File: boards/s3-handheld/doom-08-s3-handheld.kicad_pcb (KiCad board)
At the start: 4 copper layers, 156 x 66 mm, 62 parts, among them J2 S2B-PH-K-S(LF)(SN), J4 DM3AT-SF-PEJM5, J5 S2B-PH-K-S(LF)(SN), SW12 JS102011SAQN, U1 ESP32-S3-WROOM-1-N16R8, U2 ESD 2-line, U4 TLV75533PDBVR, U5 MAX98357AETE+T, U6 BQ24074RGTR, U7 MAX17048G+T10

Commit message: PCBKit's mark and pcbkit.io on every board; the RP2350 handheld ready to order
The handheld runs from two 18650 cells in parallel behind a DW01A protector and a reverse-cell
P-MOSFET, charged at up to 500 mA from the Pico's USB-C by a BQ24075 (power path into VSYS, timers
off for 6 Ah), with an on/off switch on 3V3_EN, M3 holes, ground pours and the console on pads.
Every assembled part has a JLCPCB code in stock (Basic where there is one); the module sockets are
in the BOM, the modules listed in the order's README. Check complete, the ready review clean.
Every board: routed and checked complete with the new mark.
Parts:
- added logo: , Logo_PCBKit_pcbkit.io, F.Cu at (209.5, 195.2)
- SW1, SW10, SW11, SW2, SW3, SW4, SW5, SW6, SW7, SW8, SW9: value (none) -> PTS645SM43SMTR92 LFS

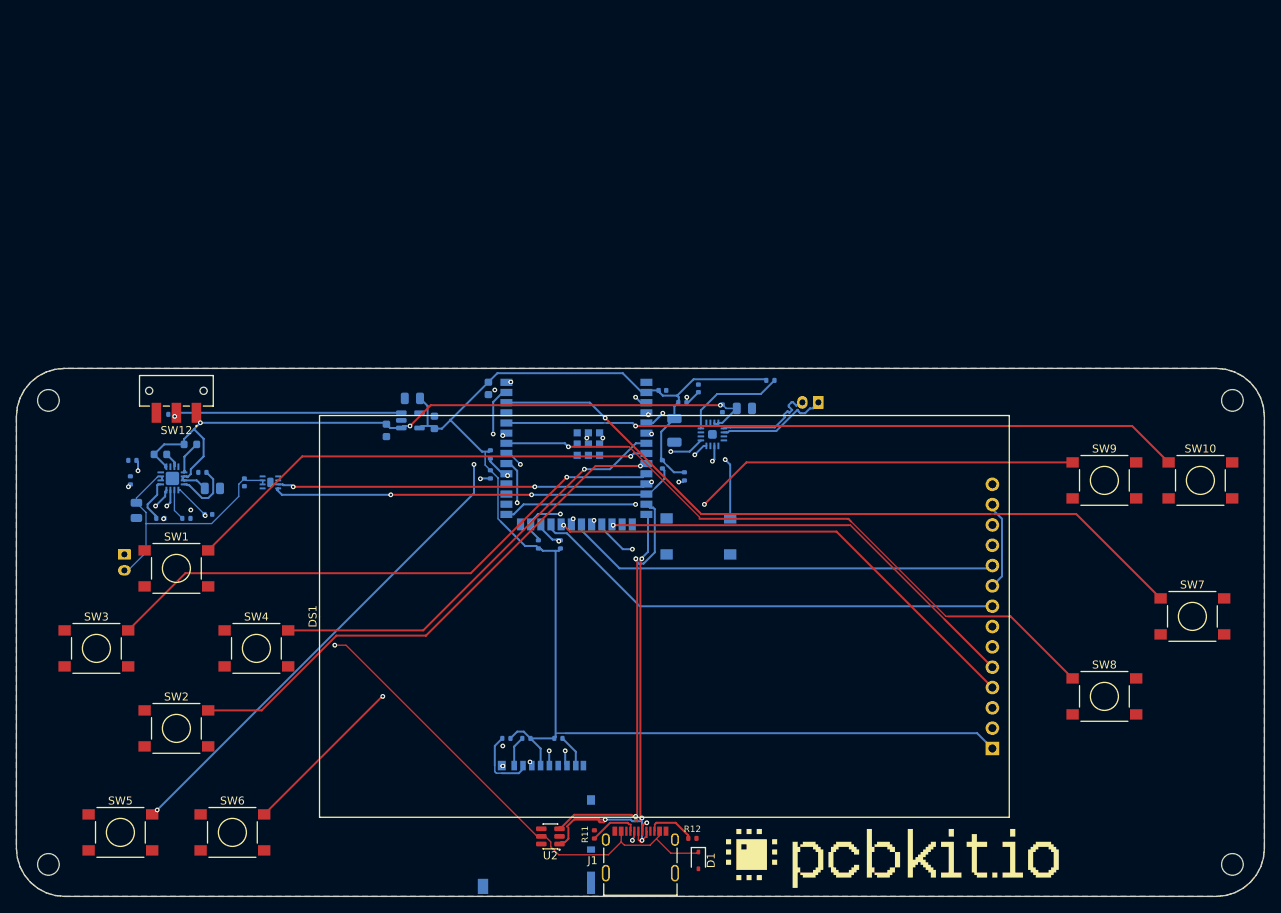
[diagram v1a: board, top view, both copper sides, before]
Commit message: s3-handheld: two 18650 cells with protection and a BQ24075 power path; every part orderable
The LiPo on a JST becomes two 18650 cells in parallel (Keystone 1042 holders on the back) behind a
reverse-cell P-FET and DW01A + FS8205A protection, charged by a BQ24075 with power path (as
boards/rp2350-handheld) in place of the BQ24074; the MAX17048 gauges the pack, the TLV75533 and the
amplifier run from SYS. USB-C moved to the back's top edge beside the module, RESET to the front
beside MENU (BOOT); the speaker connector on the bottom edge. Board 156 x 110 mm, M3 holes, test
pads; every assembled part pinned to an LCSC code.
check: complete, 0 errors, 2 warnings (USB FS pair coupling and skew, justified in the README);
ready lens: nothing to fix; fab export without --force.

Claude-Session: https://claude.ai/code/session_01ATmMmxyrWxFwR3nTdXUrcx
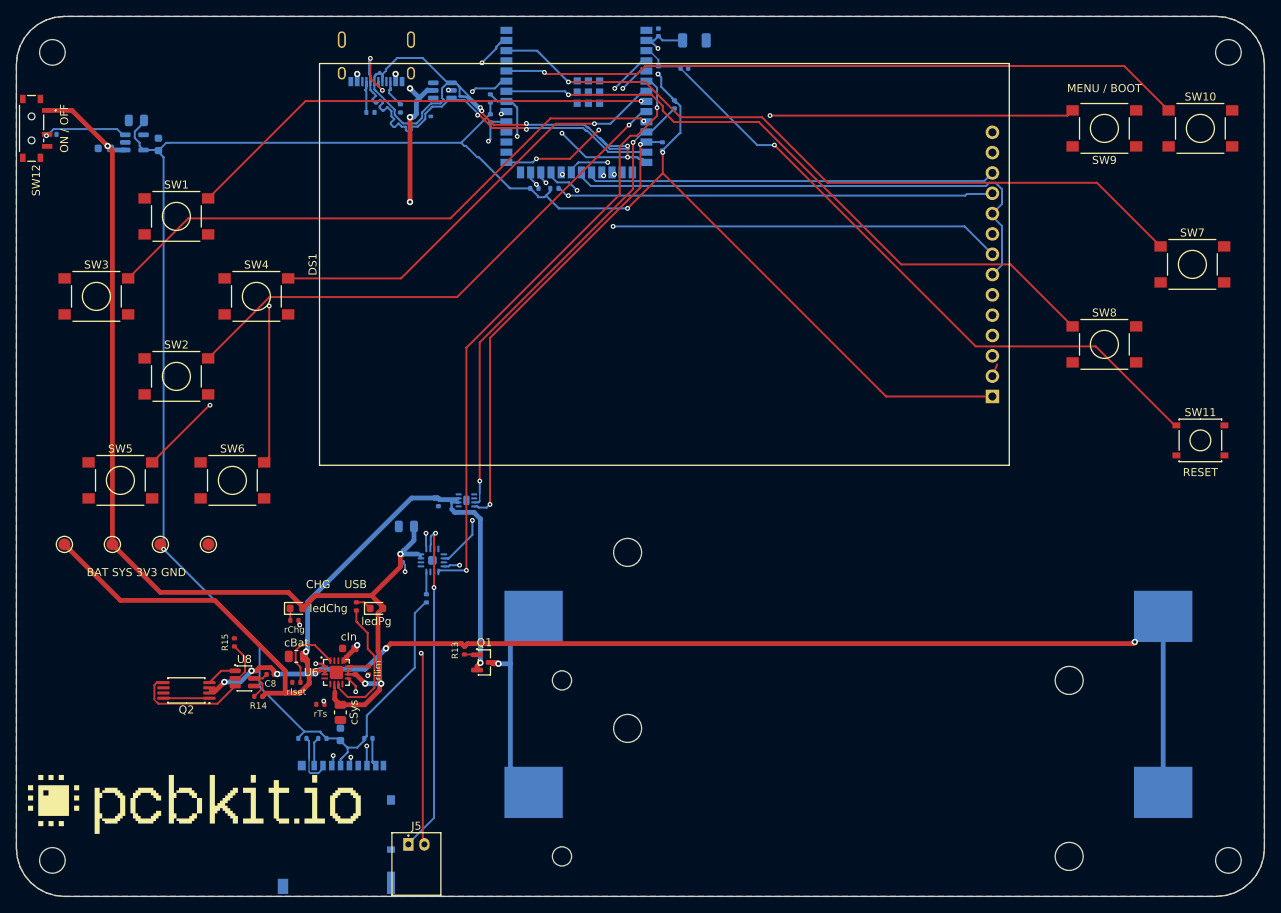
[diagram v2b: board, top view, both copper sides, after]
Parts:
- removed C10, C9: 4.7uF, C_0805_2012Metric
- removed D2: red, LED_0603_1608Metric
- removed D3: green, LED_0603_1608Metric
- removed J2: S2B-PH-K-S(LF)(SN), JST_PH_S2B-PH-K_1x02_P2.00mm_Horizontal
- removed R16: 46.4kohm, R_0402_1005Metric
- removed R17: 10kohm, R_0402_1005Metric
- added BT1: 1042, BatteryHolder_Keystone_1042_1x18650, B.Cu at (204.0, 187.0)
- added BT2: 1042, BatteryHolder_Keystone_1042_1x18650, B.Cu at (204.0, 165.0)
- added Q1: AO3401A, SOT-23, F.Cu at (158.5, 170.8)
- added Q2: FS8205A, TSSOP-8_4.4x2.93mm_P0.65mm, F.Cu at (121.2, 174.2)
- added U8: DW01A, SOT-6_1.6x2.9mm_P0.95mm, F.Cu at (128.5, 172.8)
- added cBat: 4.7uF, C_0805_2012Metric, F.Cu at (135.0, 170.0)
- added cIn: 1uF, C_0603_1608Metric, F.Cu at (141.6, 169.0)
- added cSys: 4.7uF, C_0805_2012Metric, F.Cu at (140.5, 177.0)
- added ledChg: red, LED_0603_1608Metric, F.Cu at (135.0, 164.0)
- added ledPg: green, LED_0603_1608Metric, F.Cu at (145.0, 164.0)
- added rChg: 1.5kohm, R_0402_1005Metric, F.Cu at (134.8, 165.5)
- added rIlim: 1.18kohm, R_0402_1005Metric, F.Cu at (144.0, 171.8)
- added rIset: 1.13kohm, R_0402_1005Metric, F.Cu at (135.0, 173.2)
- added rPg: 1.5kohm, R_0402_1005Metric, F.Cu at (142.5, 163.8)
- added rTs: 10kohm, R_0402_1005Metric, F.Cu at (138.0, 176.0)
- added tpBat: , TestPoint_Round_D1.5mm, F.Cu at (106.0, 156.0)
- added tpGnd: , TestPoint_Round_D1.5mm, F.Cu at (124.0, 156.0)
- added tpSys: , TestPoint_Round_D1.5mm, F.Cu at (112.0, 156.0)
- added tpV3: , TestPoint_Round_D1.5mm, F.Cu at (118.0, 156.0)
- C8: value 1uF -> 100nF; moved to F.Cu
- D1, J1, R11, R12, U2: moved to B.Cu
- H1, H2, H3, H4: footprint MountingHole_2.7mm_M2.5 -> MountingHole_3.2mm_M3
- J5: moved to F.Cu
- R13: value 1.13kohm -> 100kohm; moved to F.Cu
- R14: value 1.18kohm -> 100ohm; moved to F.Cu
- R15: value 4.12kohm -> 1kohm; moved to F.Cu
- SW11: value PTS645SM43SMTR92 LFS -> TS-1187A-B-A-B; footprint SW_Tactile_SPST_6x6mm_SMD -> SW_Tactile_SPST_5.1x5.1mm_SMD; moved to F.Cu
- SW12: value JS102011SAQN -> MSK12C02; footprint SW_Slide_SPDT_CK_JS102011SAQN_Horizontal -> SW_Slide_SPDT_Shouhan_MSK12C02
- U6: value BQ24074RGTR -> BQ24075RGTR; moved to F.Cu
- moved J1 99.3 mm to (145.0, 98.2), turned to 180 degrees
- moved D1 99.2 mm to (150.8, 102.5), turned to 180 degrees
- moved R12 98.3 mm to (148.0, 101.5), turned to 90 degrees
- moved R11 94.5 mm to (144.2, 102.0), turned to 180 degrees
- moved U2 94.2 mm to (153.2, 99.2), turned to 0 degrees
- moved logo 87.5 mm to (122.2, 188.5)
- moved J5 74.0 mm to (150.0, 193.5)
- moved SW11 63.9 mm to (248.0, 143.0)
- moved R10 50.9 mm to (151.2, 162.8), turned to 270 degrees
- moved C12 49.9 mm to (111.0, 106.5), turned to 0 degrees
- moved C13 49.0 mm to (117.8, 106.0)
- moved C2 49.0 mm to (115.0, 103.0)
- moved U4 49.0 mm to (114.8, 105.8)
- moved C3 48.8 mm to (184.8, 93.0), turned to 180 degrees
- moved C1 47.0 mm to (140.5, 179.8), turned to 270 degrees
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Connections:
- C11 pad 1: VBAT -> BAT
- C12 pad 1: VSYS -> SYS
- C6 pad 1: VSYS -> SYS
- C7 pad 1: VSYS -> SYS
- C8 pad 1: VBUS -> CELL_N
- C8 pad 2: GND -> Net-(C8-1)
- R13 pad 1: Net-(R13-1) -> reversed/gate
- R13 pad 2: GND -> CELL_N
- R14 pad 1: Net-(R14-1) -> BAT
- R14 pad 2: GND -> Net-(C8-1)
- R18 pad 1: SDA -> V3
- R18 pad 2: V3 -> SDA
- R19 pad 1: SCL -> V3
- R19 pad 2: V3 -> SCL
- R4 pad 1: V3 -> SD_D0
- R4 pad 2: SD_D0 -> V3
- R7 pad 1: V3 -> SD_D3
- R7 pad 2: SD_D3 -> V3
- R9 pad 1: EN -> V3
- R9 pad 2: V3 -> EN
- SW12 pad 1: VSYS -> SYS
- U4 pad 1: VSYS -> SYS
- U5 pad 7: VSYS -> SYS
- U5 pad 8: VSYS -> SYS
- U6 pad 1: Net-(R17-1) -> TS
- U6 pad 10: VSYS -> SYS
- U6 pad 11: VSYS -> SYS
- U6 pad 12: Net-(R14-1) -> ILIM
- U6 pad 14: Net-(R16-1) -> GND
- U6 pad 15: Net-(R15-1) -> GND
- U6 pad 16: Net-(R13-1) -> ISET
- U6 pad 2: VBAT -> BAT
- U6 pad 3: VBAT -> BAT
- U6 pad 5: VSYS -> GND
- U6 pad 6: GND -> SYS
- U6 pad 7: Net-(D3-1) -> PG_N
- U6 pad 9: Net-(D2-1) -> CHG_N
- U7 pad 2: VBAT -> BAT
- U7 pad 3: VBAT -> BAT
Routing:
- net CELL_N: track 0.00 -> 141.2 mm, vias 0 -> 5
- net SYS: track 0.00 -> 138.2 mm, vias 0 -> 4
- net BAT: track 0.00 -> 107.2 mm, vias 0 -> 2
- net V3: track 179.7 -> 274.2 mm, vias 0 -> 5
- net VSYS: track 94.4 -> 0.00 mm, vias 3 -> 0
- net I2S_DIN: track 7.65 -> 77.0 mm
- net I2S_BCK: track 9.78 -> 75.0 mm
- net I2S_LRCK: track 13.3 -> 72.4 mm
- net EN: track 28.1 -> 86.9 mm, vias 3 -> 1
- net BAT_IN: track 0.00 -> 55.6 mm, vias 0 -> 1
- net SD_CMD: track 40.0 -> 90.6 mm
- net SD_CLK: track 40.2 -> 89.3 mm
- net SD_D0: track 49.4 -> 94.1 mm, vias 3 -> 2
- net VBAT: track 34.1 -> 0.00 mm
- net DP: track 62.7 -> 96.5 mm, vias 4 -> 6
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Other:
- board size 156 x 66 mm -> 156 x 110 mm
- board text added: "+"
- board text added: "-"
- board text added: "2 x 18650 Li-ion 3.7 V"
- board text added: "BAT SYS 3V3 GND"
- board text added: "CHG USB"
- board text added: "MENU / BOOT"
- board text added: "ON / OFF"
- board text added: "RESET"
